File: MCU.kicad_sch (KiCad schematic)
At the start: 13 parts, among them J2 AVR-ISP-6, J3 USB_B, U3 ATmega2560-16A, Y1 16MHz

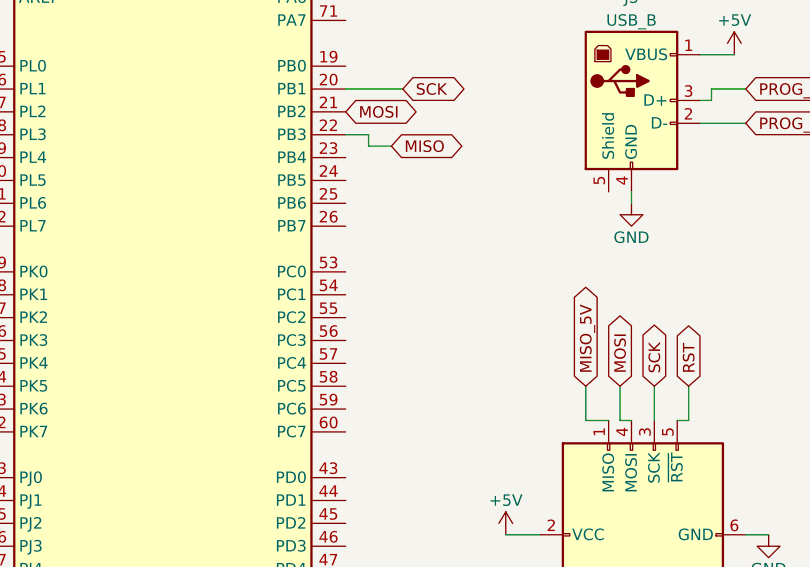
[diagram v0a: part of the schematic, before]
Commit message: "Resolved the issue of SS34 diode footprint. Problem was the pin on the downloaded footprint were not numbered
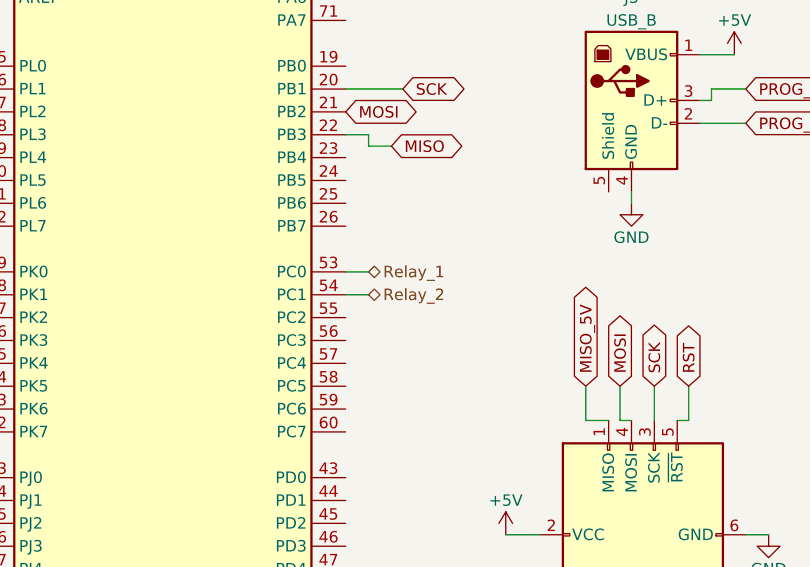
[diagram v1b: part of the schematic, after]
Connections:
- net Relay_1: now reaches U3.53 (PC0)
- net Relay_2: now reaches U3.54 (PC1)
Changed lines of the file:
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@@
+    (stroke (width 0) (type default))
+  )
+  (wire (pts (xy 138.43 91.44) (xy 140.97 91.44))
     (stroke (width 0) (type default))
   )
@@
   )
   (wire (pts (xy 106.68 26.67) (xy 115.57 26.67))
+    (stroke (width 0) (type default))
+  )
+  (wire (pts (xy 138.43 88.9) (xy 140.97 88.9))
     (stroke (width 0) (type default))
   )
@@
     (effects (font (size 1.27 1.27)) (justify right))
   )
+  (hierarchical_label "Relay_1" (shape bidirectional) (at 140.97 88.9 0) (fields_autoplaced)
+    (effects (font (size 1.27 1.27)) (justify left))
+  )
   (hierarchical_label "+5V" (shape bidirectional) (at 102.87 33.02 180) (fields_autoplaced)
     (effects (font (size 1.27 1.27)) (justify right))
   )
+  (hierarchical_label "Relay_2" (shape bidirectional) (at 140.97 91.44 0) (fields_autoplaced)
+    (effects (font (size 1.27 1.27)) (justify left))
+  )
   (symbol (lib_id "power:GND") (at 118.11 186.69 0) (unit 1)

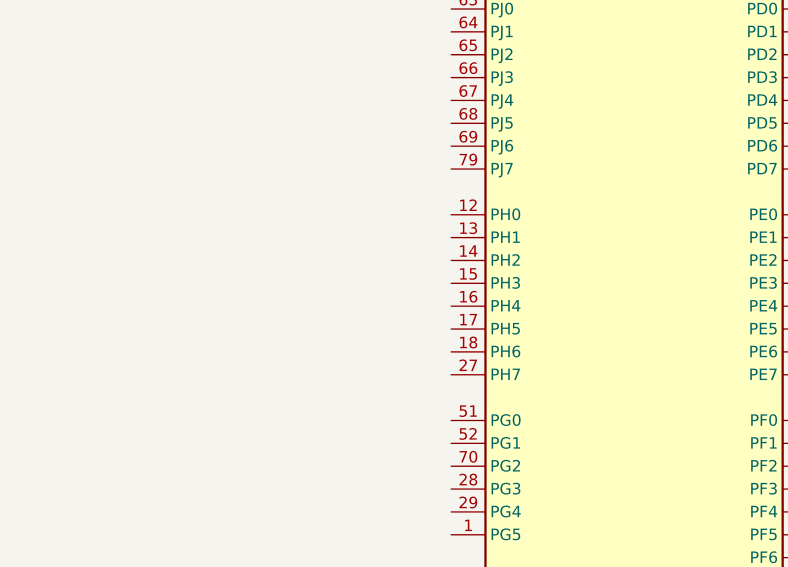
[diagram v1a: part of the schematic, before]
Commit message: Added DC motor driver
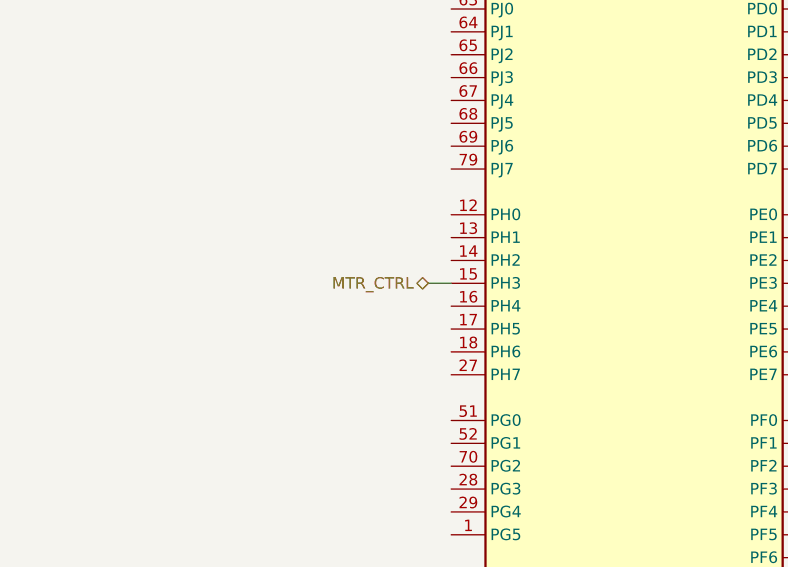
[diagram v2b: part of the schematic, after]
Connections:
- net MTR_CTRL: now reaches U3.15 (PH3)
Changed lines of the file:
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@@
+    (stroke (width 0) (type default))
+  )
+  (wire (pts (xy 95.25 142.24) (xy 97.79 142.24))
     (stroke (width 0) (type default))
   )
@@
     (effects (font (size 1.27 1.27)) (justify right))
   )
+  (hierarchical_label "MTR_CTRL" (shape bidirectional) (at 95.25 142.24 180) (fields_autoplaced)
+    (effects (font (size 1.27 1.27)) (justify right))
+  )

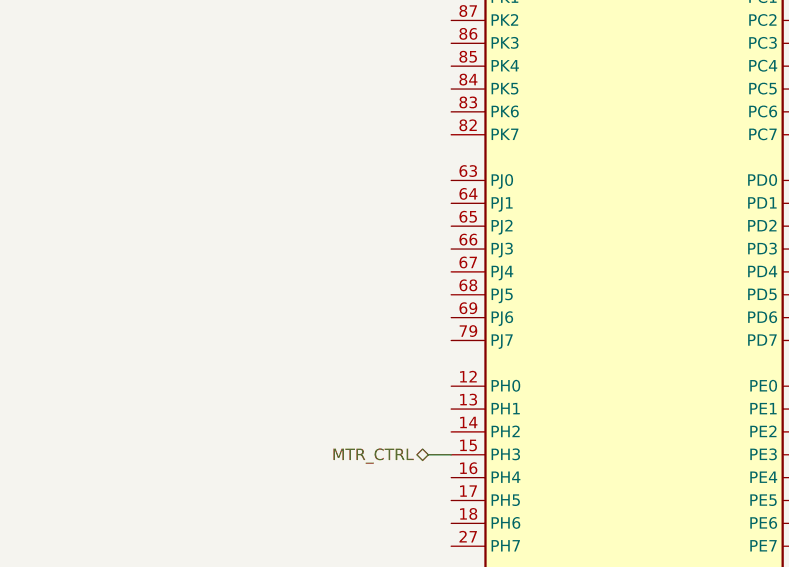
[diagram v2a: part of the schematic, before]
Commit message: Designed circuit for reading digital input. CHY74 (4 channel optocoupler) used
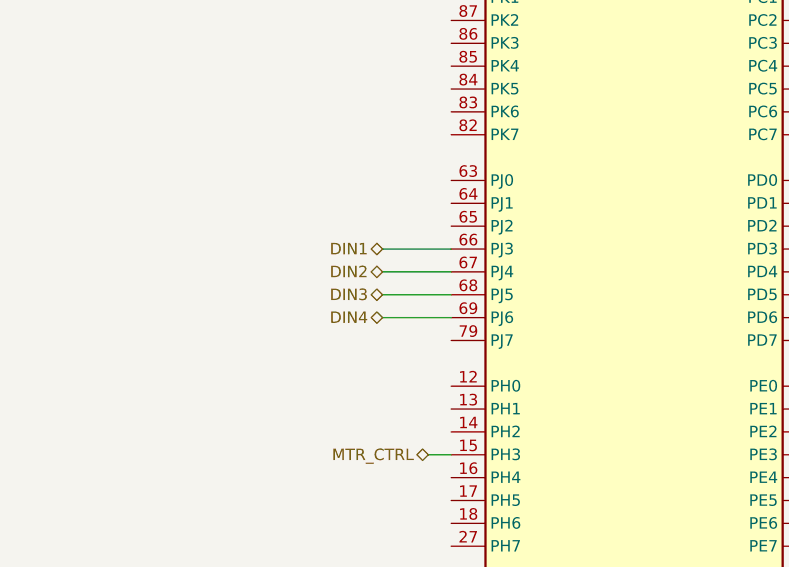
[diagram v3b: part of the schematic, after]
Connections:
- net DIN1: now reaches U3.66 (PJ3)
- net DIN2: now reaches U3.67 (PJ4)
- net DIN3: now reaches U3.68 (PJ5)
- net DIN4: now reaches U3.69 (PJ6)
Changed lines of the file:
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@@
+    (stroke (width 0) (type default))
+  )
+  (wire (pts (xy 90.17 121.92) (xy 97.79 121.92))
+    (stroke (width 0) (type default))
+  )
+  (wire (pts (xy 90.17 119.38) (xy 97.79 119.38))
     (stroke (width 0) (type default))
   )
@@
     (stroke (width 0) (type default))
   )
+  (wire (pts (xy 90.17 124.46) (xy 97.79 124.46))
+    (stroke (width 0) (type default))
+  )
   (wire (pts (xy 179.07 69.85) (xy 177.8 69.85))
     (stroke (width 0) (type default))
@@
     (stroke (width 0) (type default))
   )
+  (wire (pts (xy 90.17 127) (xy 97.79 127))
+    (stroke (width 0) (type default))
+  )
   (wire (pts (xy 102.87 33.02) (xy 106.68 33.02))
     (stroke (width 0) (type default))
@@
     )
   )
+  (hierarchical_label "DIN2" (shape bidirectional) (at 90.17 121.92 180) (fields_autoplaced)
+    (effects (font (size 1.27 1.27)) (justify right))
+  )
+  (hierarchical_label "DIN4" (shape bidirectional) (at 90.17 127 180) (fields_autoplaced)
+    (effects (font (size 1.27 1.27)) (justify right))
+  )
   (hierarchical_label "GND" (shape bidirectional) (at 118.11 184.15 180) (fields_autoplaced)
     (effects (font (size 1.27 1.27)) (justify right))
   )
+  (hierarchical_label "DIN3" (shape bidirectional) (at 90.17 124.46 180) (fields_autoplaced)
+    (effects (font (size 1.27 1.27)) (justify right))
+  )
   (hierarchical_label "Relay_1" (shape bidirectional) (at 140.97 88.9 0) (fields_autoplaced)
     (effects (font (size 1.27 1.27)) (justify left))
   )
+  (hierarchical_label "DIN1" (shape bidirectional) (at 90.17 119.38 180) (fields_autoplaced)
+    (effects (font (size 1.27 1.27)) (justify right))
+  )
   (hierarchical_label "+5V" (shape bidirectional) (at 102.87 33.02 180) (fields_autoplaced)

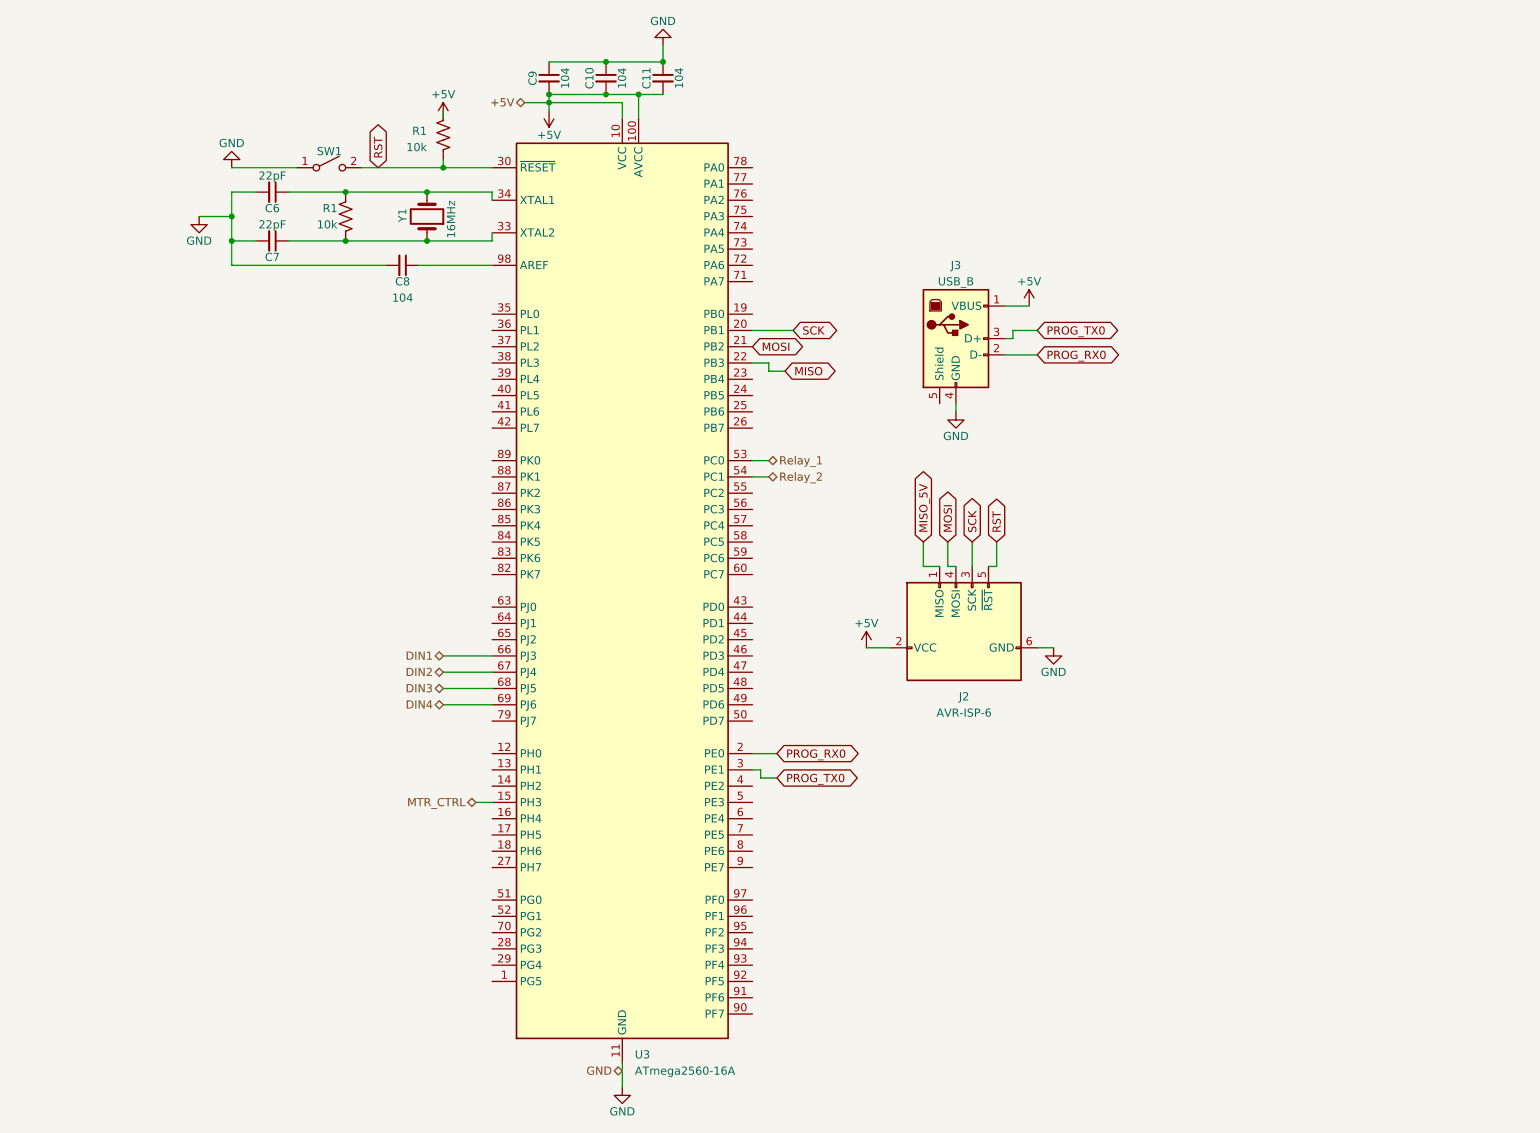
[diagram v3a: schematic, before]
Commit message: Analog input schematic
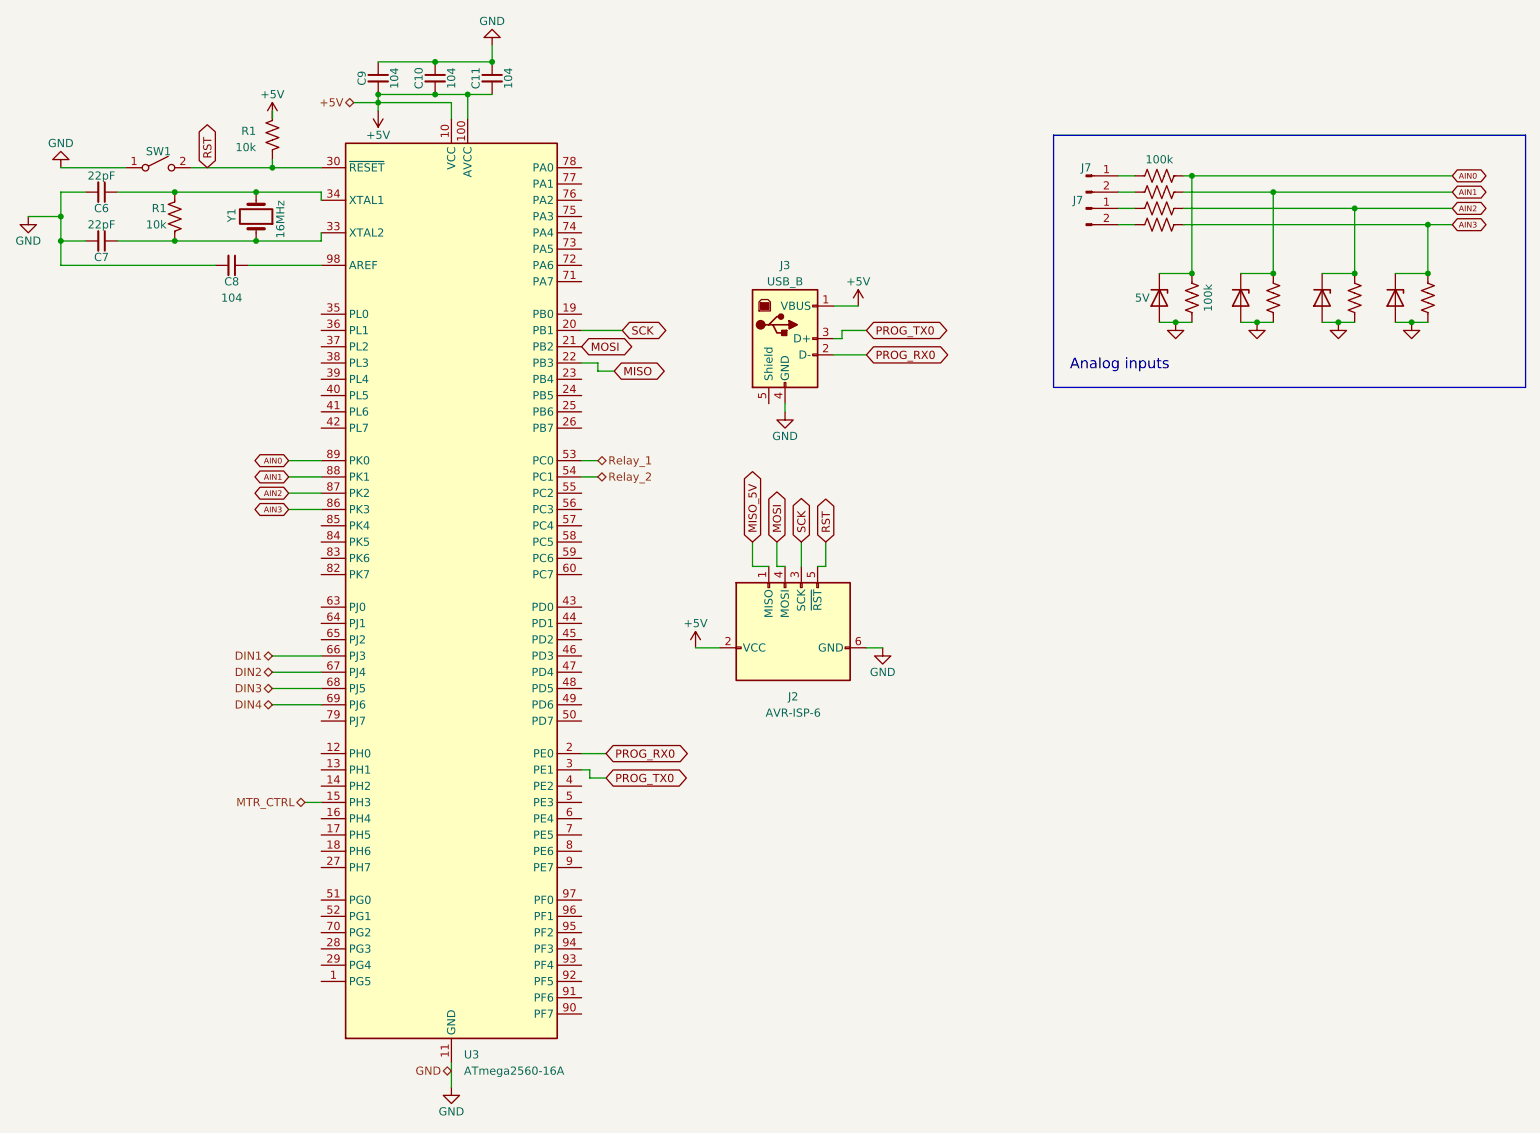
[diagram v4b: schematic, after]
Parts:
- added D13, D14, D15, D16: 5V, Diode_SMD:D_SOD-323_HandSoldering, symbol Device:D_Zener
- added J7 (x2): Screw, Connector_Phoenix_MSTB:PhoenixContact_MSTBA_2,5_2-G-5,08_1x02_P5.08mm_Horizontal, symbol Connector:Conn_01x02_Pin
- added R21, R22, R24, R25, R26, R27, R28: 100k, Resistor_SMD:R_1206_3216Metric, symbol Device:R_US
- added R23: 100k, symbol Device:R_US
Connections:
- net GND: now also D13.2 (A), D14.2 (A), D15.2 (A), D16.2 (A), R22.1, R26.1, R27.1, R28.1
- net AIN3: now reaches U3.86 (PK3)
- net AIN3: now also D15.1 (K), R25.2, R28.2
- net AIN2: now reaches U3.87 (PK2)
- net AIN2: now also D13.1 (K), R24.2, R27.2
- net AIN1: now reaches U3.88 (PK1)
- net AIN1: now also D14.1 (K), R21.2, R26.2
- net AIN0: now reaches U3.89 (PK0)
- net AIN0: now also D16.1 (K), R22.2, R23.2
- new net: J7.1 (Pin_1), R23.1
- new net: J7.2 (Pin_2), R21.1
- new net: J7.2 (Pin_2), R25.1
- new net: J7.1 (Pin_1), R24.1
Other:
- note added: "Analog inputs"
- moved on the sheet: C10, C11, C6, C7, C8, C9, J2, J3, R1, SW1, U3, Y1
